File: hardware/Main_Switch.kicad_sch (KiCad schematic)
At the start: 6 parts

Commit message: Nightly update
Update Driver and Main_Switch.
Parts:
- added R? (x10): (no value), symbol Basic_passive_components:Resistor
- L?: value Power_Inductor -> (none)
- Q? (x4): value NTMFS5C670NL -> (none); footprint POWER_TRANSISTOR_SMD:SON-8_5x6_M -> (none)
- R?: value Resistor -> (none)
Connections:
- net BG1: now also R?.1; no longer Q?.G (Gate)
- net BG2: now also R?.2; no longer Q?.G (Gate)
- net GND: now also Q?.S (Source), Q?.S (Source), R?.1, R?.1
- net TG1: now also R?.1; no longer Q?.G (Gate)
- net TG2: now also R?.2; no longer Q?.G (Gate)
- net VBUS: now also Q?.D (Drain)
- net VDC: now also Q?.D (Drain)
- net SW2: now reaches Q?.D (Drain), Q?.S (Source), R?.2
- net SW2: now also R?.1, R?.2
- net SW1: now reaches L?.1, Q?.D (Drain), Q?.S (Source)
- net SW1: now also R?.1
- net at L?.2, R?.1: now also R?.2
- new net: Q?.G (Gate), R?.1, R?.2 (x2)
- new net: Q?.G (Gate), R?.2, R?.2 (x2)
- new net CS_N: R?.1
- new net CS_P: R?.1
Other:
- moved on the sheet: Q?

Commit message: Nightly update
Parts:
- L?: value (none) -> 4.7uH; footprint (none) -> POWER_INDUCTOR_SMD:MC-1770
- Q? (x4): value (none) -> NTMFS5C670NL; footprint (none) -> POWER_TRANSISTOR_SMD:SON-8_5x6_M
- R? (x4): value (none) -> 10kR; footprint (none) -> GENERAL_RCL_SMD:R0603(1608M)
- R? (x2): value (none) -> 0R; footprint (none) -> GENERAL_RCL_SMD:R0402(1005M)
- R? (x4): value (none) -> 5.1R; footprint (none) -> GENERAL_RCL_SMD:R0603(1608M)
- R?: value (none) -> 10mR; footprint (none) -> GENERAL_RCL_SMD:R2512(6332M)
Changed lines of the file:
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@@
       (effects (font (size 1.27 1.27)) (justify left))
     )
-    (property "Value" "" (id 1) (at 175.26 102.8699 0)
-      (effects (font (size 1.27 1.27)) (justify left))
-    )
-    (property "Footprint" "" (id 2) (at 156.21 97.79 0)
+    (property "Value" "NTMFS5C670NL" (id 1) (at 175.26 102.8699 0)
+      (effects (font (size 1.27 1.27)) (justify left))
+    )
+    (property "Footprint" "POWER_TRANSISTOR_SMD:SON-8_5x6_M" (id 2) (at 156.21 97.79 0)
       (effects (font (size 1.27 1.27)) hide)
     )
@@
       (effects (font (size 1.27 1.27)) (justify right))
     )
-    (property "Value" "" (id 1) (at 96.52 110.4899 90)
-      (effects (font (size 1.27 1.27)) (justify right))
-    )
-    (property "Footprint" "" (id 2) (at 90.17 113.03 0)
+    (property "Value" "10kR" (id 1) (at 96.52 110.4899 90)
+      (effects (font (size 1.27 1.27)) (justify right))
+    )
+    (property "Footprint" "GENERAL_RCL_SMD:R0603(1608M)" (id 2) (at 90.17 113.03 0)
       (effects (font (size 1.27 1.27)) hide)
     )
@@
     (in_bom yes) (on_board yes) (fields_autoplaced)
     (property "Reference" "R?" (id 0) (at 137.16 105.41 0))
-    (property "Value" "" (id 1) (at 137.16 107.95 0))
-    (property "Footprint" "" (id 2) (at 133.35 107.95 0)
+    (property "Value" "0R" (id 1) (at 137.16 107.95 0))
+    (property "Footprint" "GENERAL_RCL_SMD:R0402(1005M)" (id 2) (at 133.35 107.95 0)
       (effects (font (size 1.27 1.27)) hide)
     )
@@
       (effects (font (size 1.27 1.27)) (justify right))
     )
-    (property "Value" "" (id 1) (at 96.52 72.3899 90)
-      (effects (font (size 1.27 1.27)) (justify right))
-    )
-    (property "Footprint" "" (id 2) (at 90.17 74.93 0)
+    (property "Value" "10kR" (id 1) (at 96.52 72.3899 90)
+      (effects (font (size 1.27 1.27)) (justify right))
+    )
+    (property "Footprint" "GENERAL_RCL_SMD:R0603(1608M)" (id 2) (at 90.17 74.93 0)
       (effects (font (size 1.27 1.27)) hide)
     )
@@
       (effects (font (size 1.27 1.27)) (justify left))
     )
-    (property "Value" "" (id 1) (at 104.14 64.7699 0)
-      (effects (font (size 1.27 1.27)) (justify left))
-    )
-    (property "Footprint" "" (id 2) (at 123.19 59.69 0)
+    (property "Value" "NTMFS5C670NL" (id 1) (at 104.14 64.7699 0)
+      (effects (font (size 1.27 1.27)) (justify left))
+    )
+    (property "Footprint" "POWER_TRANSISTOR_SMD:SON-8_5x6_M" (id 2) (at 123.19 59.69 0)
       (effects (font (size 1.27 1.27)) hide)
     )
@@
       (effects (font (size 1.27 1.27)) (justify left))
     )
-    (property "Value" "" (id 1) (at 175.26 64.7699 0)
-      (effects (font (size 1.27 1.27)) (justify left))
-    )
-    (property "Footprint" "" (id 2) (at 156.21 59.69 0)
+    (property "Value" "NTMFS5C670NL" (id 1) (at 175.26 64.7699 0)
+      (effects (font (size 1.27 1.27)) (justify left))
+    )
+    (property "Footprint" "POWER_TRANSISTOR_SMD:SON-8_5x6_M" (id 2) (at 156.21 59.69 0)
       (effects (font (size 1.27 1.27)) hide)
     )
@@
     (in_bom yes) (on_board yes) (fields_autoplaced)
     (property "Reference" "R?" (id 0) (at 195.58 95.25 0))
-    (property "Value" "" (id 1) (at 195.58 97.79 0))
-    (property "Footprint" "" (id 2) (at 191.77 97.79 0)
+    (property "Value" "5.1R" (id 1) (at 195.58 97.79 0))
+    (property "Footprint" "GENERAL_RCL_SMD:R0603(1608M)" (id 2) (at 191.77 97.79 0)
       (effects (font (size 1.27 1.27)) hide)
     )
@@
       (effects (font (size 1.27 1.27)) (justify left))
     )
-    (property "Value" "" (id 1) (at 104.14 102.8699 0)
-      (effects (font (size 1.27 1.27)) (justify left))
-    )
-    (property "Footprint" "" (id 2) (at 123.19 97.79 0)
+    (property "Value" "NTMFS5C670NL" (id 1) (at 104.14 102.8699 0)
+      (effects (font (size 1.27 1.27)) (justify left))
+    )
+    (property "Footprint" "POWER_TRANSISTOR_SMD:SON-8_5x6_M" (id 2) (at 123.19 97.79 0)
       (effects (font (size 1.27 1.27)) hide)
     )
@@
       (effects (font (size 1.27 1.27)) (justify right))
     )
-    (property "Value" "" (id 1) (at 190.5 110.4899 90)
-      (effects (font (size 1.27 1.27)) (justify right))
-    )
-    (property "Footprint" "" (id 2) (at 184.15 113.03 0)
+    (property "Value" "10kR" (id 1) (at 190.5 110.4899 90)
+      (effects (font (size 1.27 1.27)) (justify right))
+    )
+    (property "Footprint" "GENERAL_RCL_SMD:R0603(1608M)" (id 2) (at 184.15 113.03 0)
       (effects (font (size 1.27 1.27)) hide)
     )
@@
     (in_bom yes) (on_board yes) (fields_autoplaced)
     (property "Reference" "L?" (id 0) (at 127 82.55 0))
-    (property "Value" "" (id 1) (at 127 85.09 0))
-    (property "Footprint" "" (id 2) (at 127 88.9 0)
+    (property "Value" "4.7uH" (id 1) (at 127 85.09 0))
+    (property "Footprint" "POWER_INDUCTOR_SMD:MC-1770" (id 2) (at 127 88.9 0)
       (effects (font (size 1.27 1.27)) hide)
     )
@@
       (effects (font (size 1.27 1.27)) hide)
     )
-    (property "Value" "" (id 1) (at 177.8 132.08 0))
+    (property "Value" "GND" (id 1) (at 177.8 132.08 0))
     (property "Footprint" "" (id 2) (at 177.8 127 0)
       (effects (font (size 1.27 1.27)) hide)
@@
     (in_bom yes) (on_board yes) (fields_autoplaced)
     (property "Reference" "R?" (id 0) (at 83.82 57.15 0))
-    (property "Value" "" (id 1) (at 83.82 59.69 0))
-    (property "Footprint" "" (id 2) (at 80.01 59.69 0)
+    (property "Value" "5.1R" (id 1) (at 83.82 59.69 0))
+    (property "Footprint" "GENERAL_RCL_SMD:R0603(1608M)" (id 2) (at 80.01 59.69 0)
       (effects (font (size 1.27 1.27)) hide)
     )
@@
     (in_bom yes) (on_board yes) (fields_autoplaced)
     (property "Reference" "R?" (id 0) (at 137.16 95.25 0))
-    (property "Value" "" (id 1) (at 137.16 97.79 0))
-    (property "Footprint" "" (id 2) (at 133.35 97.79 0)
+    (property "Value" "0R" (id 1) (at 137.16 97.79 0))
+    (property "Footprint" "GENERAL_RCL_SMD:R0402(1005M)" (id 2) (at 133.35 97.79 0)
       (effects (font (size 1.27 1.27)) hide)
     )
@@
       (effects (font (size 1.27 1.27)) hide)
     )
-    (property "Value" "" (id 1) (at 101.6 45.72 0))
+    (property "Value" "VDC" (id 1) (at 101.6 45.72 0))
     (property "Footprint" "" (id 2) (at 101.6 50.8 0)
       (effects (font (size 1.27 1.27)) hide)
@@
     (in_bom yes) (on_board yes) (fields_autoplaced)
     (property "Reference" "R?" (id 0) (at 152.4 82.55 0))
-    (property "Value" "" (id 1) (at 152.4 85.09 0))
-    (property "Footprint" "" (id 2) (at 148.59 85.09 0)
+    (property "Value" "10mR" (id 1) (at 152.4 85.09 0))
+    (property "Footprint" "GENERAL_RCL_SMD:R2512(6332M)" (id 2) (at 148.59 85.09 0)
       (effects (font (size 1.27 1.27)) hide)
     )
@@
       (effects (font (size 1.27 1.27)) hide)
     )
-    (property "Value" "" (id 1) (at 177.8 45.72 0))
+    (property "Value" "VBUS" (id 1) (at 177.8 45.72 0))
     (property "Footprint" "" (id 2) (at 177.8 50.8 0)
       (effects (font (size 1.27 1.27)) hide)
@@
     (in_bom yes) (on_board yes) (fields_autoplaced)
     (property "Reference" "R?" (id 0) (at 195.58 57.15 0))
-    (property "Value" "" (id 1) (at 195.58 59.69 0))
-    (property "Footprint" "" (id 2) (at 191.77 59.69 0)
+    (property "Value" "5.1R" (id 1) (at 195.58 59.69 0))
+    (property "Footprint" "GENERAL_RCL_SMD:R0603(1608M)" (id 2) (at 191.77 59.69 0)
       (effects (font (size 1.27 1.27)) hide)
     )
@@
       (effects (font (size 1.27 1.27)) (justify right))
     )
-    (property "Value" "" (id 1) (at 190.5 72.3899 90)
-      (effects (font (size 1.27 1.27)) (justify right))
-    )
-    (property "Footprint" "" (id 2) (at 184.15 74.93 0)
+    (property "Value" "10kR" (id 1) (at 190.5 72.3899 90)
+      (effects (font (size 1.27 1.27)) (justify right))
+    )
+    (property "Footprint" "GENERAL_RCL_SMD:R0603(1608M)" (id 2) (at 184.15 74.93 0)
       (effects (font (size 1.27 1.27)) hide)
     )
@@
     (in_bom yes) (on_board yes) (fields_autoplaced)
     (property "Reference" "R?" (id 0) (at 83.82 95.25 0))
-    (property "Value" "" (id 1) (at 83.82 97.79 0))
-    (property "Footprint" "" (id 2) (at 80.01 97.79 0)
+    (property "Value" "5.1R" (id 1) (at 83.82 97.79 0))
+    (property "Footprint" "GENERAL_RCL_SMD:R0603(1608M)" (id 2) (at 80.01 97.79 0)
       (effects (font (size 1.27 1.27)) hide)
     )
@@
       (effects (font (size 1.27 1.27)) hide)
     )
-    (property "Value" "" (id 1) (at 101.6 132.08 0))
+    (property "Value" "GND" (id 1) (at 101.6 132.08 0))
     (property "Footprint" "" (id 2) (at 101.6 127 0)
       (effects (font (size 1.27 1.27)) hide)

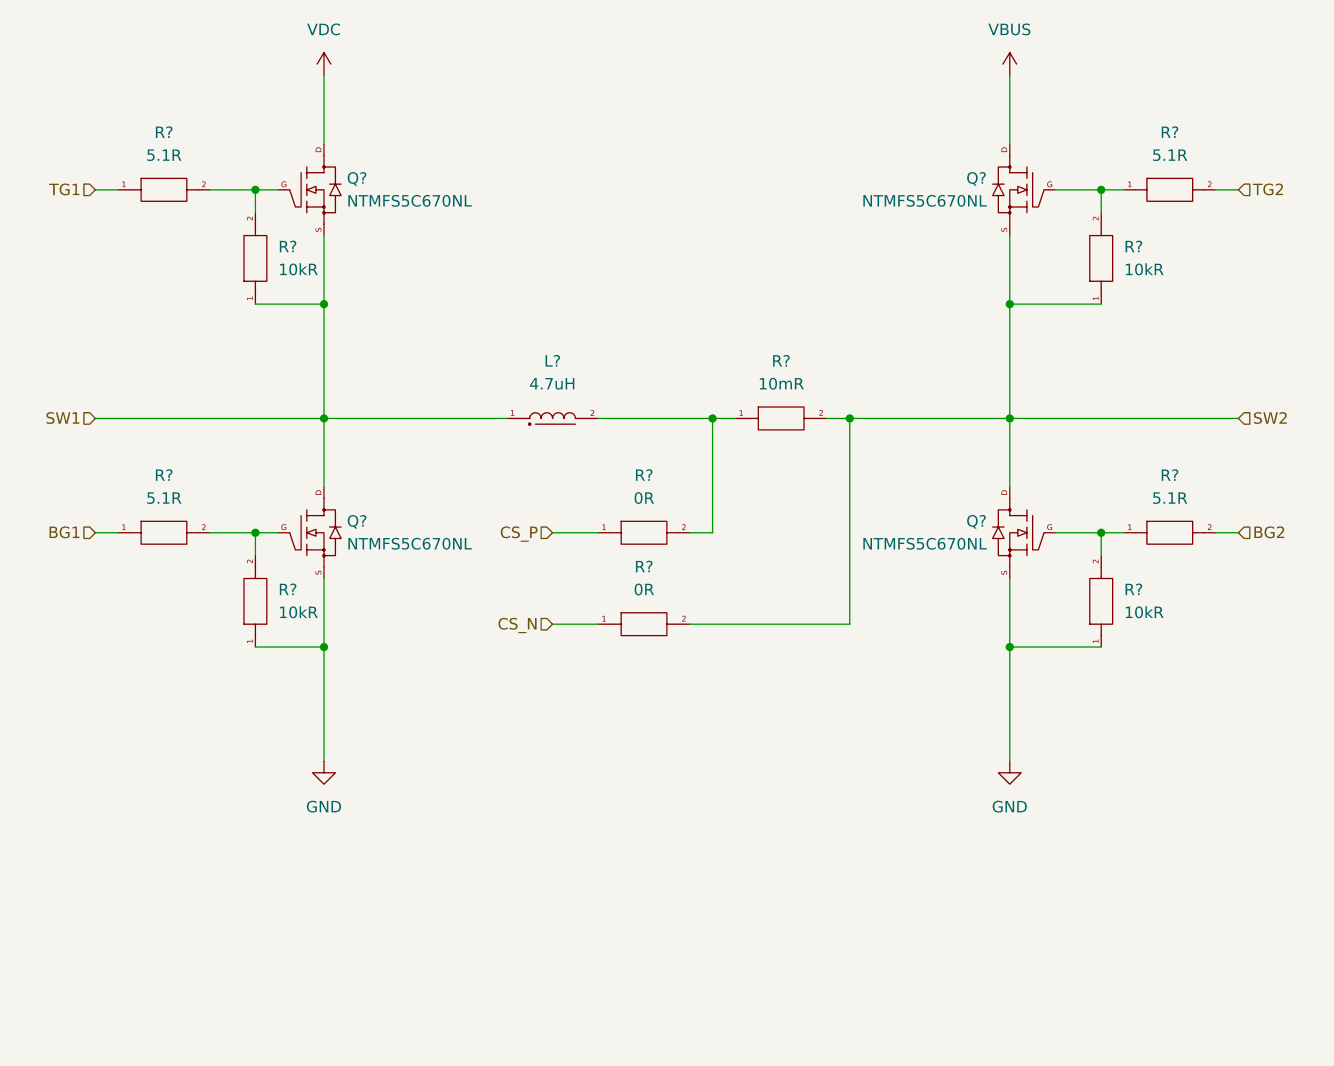
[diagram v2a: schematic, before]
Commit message: Update symbols
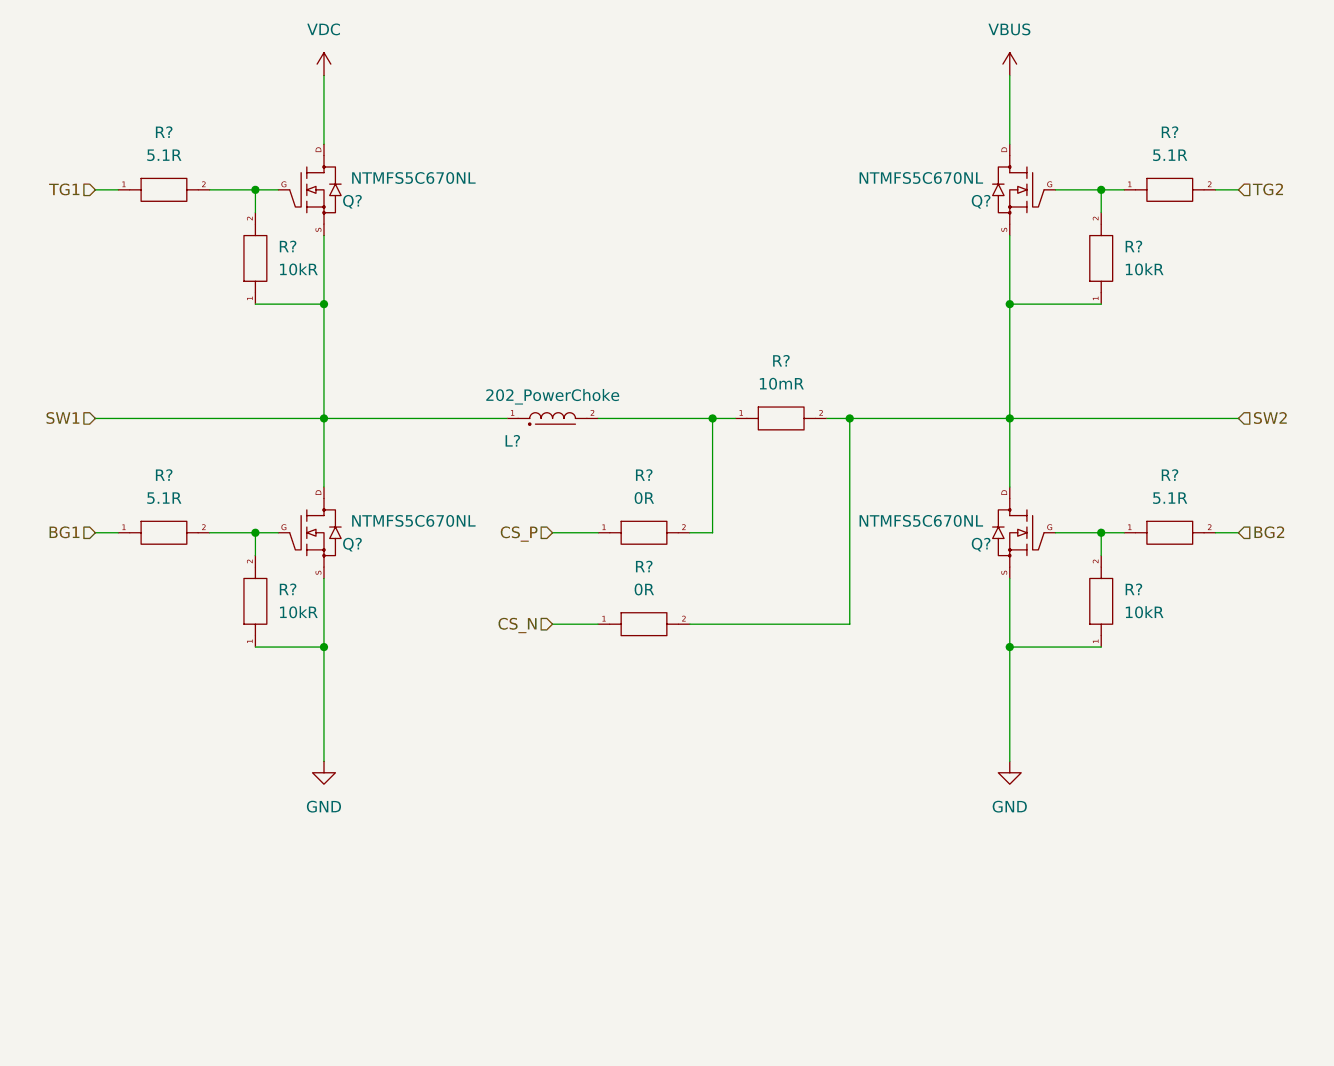
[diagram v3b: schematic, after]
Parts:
- L?: value 4.7uH -> 202_PowerChoke; symbol Basic_passive_components:Power_Inductor -> 001_Basic_PassiveComponents:202_PowerChoke; Symbol type (none) -> Alternate Source
- Q? (x4): footprint POWER_TRANSISTOR_SMD:SON-8_5x6_M -> 103_SP_POWER_TRANSISTOR_SMD:SON-6050-FET; symbol Power_transistor:NTMFS5C670NL -> 202_Power_Transistor:NTMFS5C670NL; Symbol type (none) -> Specified Device
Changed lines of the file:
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@@
     (effects (font (size 1.27 1.27)) (justify left))
   )
-  (symbol (lib_id "Power_transistor:NTMFS5C670NL") (at 177.8 101.6 0) (mirror y) (unit 1)
+  (symbol (lib_id "202_Power_Transistor:NTMFS5C670NL") (at 177.8 101.6 0) (mirror y) (unit 1)
     (in_bom yes) (on_board yes) (fields_autoplaced)
-    (property "Reference" "Q?" (id 0) (at 175.26 100.3299 0)
-      (effects (font (size 1.27 1.27)) (justify left))
-    )
-    (property "Value" "NTMFS5C670NL" (id 1) (at 175.26 102.8699 0)
-      (effects (font (size 1.27 1.27)) (justify left))
-    )
-    (property "Footprint" "POWER_TRANSISTOR_SMD:SON-8_5x6_M" (id 2) (at 156.21 97.79 0)
+    (property "Reference" "Q?" (id 0) (at 174.625 102.87 0))
+    (property "Value" "NTMFS5C670NL" (id 1) (at 167.894 100.33 0))
+    (property "Footprint" "103_SP_POWER_TRANSISTOR_SMD:SON-6050-FET" (id 2) (at 151.13 97.79 0)
       (effects (font (size 1.27 1.27)) hide)
     )
     (property "Datasheet" "" (id 3) (at 177.165 101.6 0)
+      (effects (font (size 1.27 1.27)) hide)
+    )
+    (property "Symbol type" "Specified Device" (id 4) (at 167.64 95.25 0)
       (effects (font (size 1.27 1.27)) hide)
     )
@@
     (pin "2")
   )
-  (symbol (lib_id "Power_transistor:NTMFS5C670NL") (at 101.6 63.5 0) (unit 1)
+  (symbol (lib_id "202_Power_Transistor:NTMFS5C670NL") (at 101.6 63.5 0) (unit 1)
     (in_bom yes) (on_board yes) (fields_autoplaced)
-    (property "Reference" "Q?" (id 0) (at 104.14 62.2299 0)
-      (effects (font (size 1.27 1.27)) (justify left))
-    )
-    (property "Value" "NTMFS5C670NL" (id 1) (at 104.14 64.7699 0)
-      (effects (font (size 1.27 1.27)) (justify left))
-    )
-    (property "Footprint" "POWER_TRANSISTOR_SMD:SON-8_5x6_M" (id 2) (at 123.19 59.69 0)
+    (property "Reference" "Q?" (id 0) (at 104.775 64.77 0))
+    (property "Value" "NTMFS5C670NL" (id 1) (at 111.506 62.23 0))
+    (property "Footprint" "103_SP_POWER_TRANSISTOR_SMD:SON-6050-FET" (id 2) (at 128.27 59.69 0)
       (effects (font (size 1.27 1.27)) hide)
     )
     (property "Datasheet" "" (id 3) (at 102.235 63.5 0)
+      (effects (font (size 1.27 1.27)) hide)
+    )
+    (property "Symbol type" "Specified Device" (id 4) (at 111.76 57.15 0)
       (effects (font (size 1.27 1.27)) hide)
     )
@@
     (pin "S")
   )
-  (symbol (lib_id "Power_transistor:NTMFS5C670NL") (at 177.8 63.5 0) (mirror y) (unit 1)
+  (symbol (lib_id "202_Power_Transistor:NTMFS5C670NL") (at 177.8 63.5 0) (mirror y) (unit 1)
     (in_bom yes) (on_board yes) (fields_autoplaced)
-    (property "Reference" "Q?" (id 0) (at 175.26 62.2299 0)
-      (effects (font (size 1.27 1.27)) (justify left))
-    )
-    (property "Value" "NTMFS5C670NL" (id 1) (at 175.26 64.7699 0)
-      (effects (font (size 1.27 1.27)) (justify left))
-    )
-    (property "Footprint" "POWER_TRANSISTOR_SMD:SON-8_5x6_M" (id 2) (at 156.21 59.69 0)
+    (property "Reference" "Q?" (id 0) (at 174.625 64.77 0))
+    (property "Value" "NTMFS5C670NL" (id 1) (at 167.894 62.23 0))
+    (property "Footprint" "103_SP_POWER_TRANSISTOR_SMD:SON-6050-FET" (id 2) (at 151.13 59.69 0)
       (effects (font (size 1.27 1.27)) hide)
     )
     (property "Datasheet" "" (id 3) (at 177.165 63.5 0)
+      (effects (font (size 1.27 1.27)) hide)
+    )
+    (property "Symbol type" "Specified Device" (id 4) (at 167.64 57.15 0)
       (effects (font (size 1.27 1.27)) hide)
     )
@@
     (pin "2")
   )
-  (symbol (lib_id "Power_transistor:NTMFS5C670NL") (at 101.6 101.6 0) (unit 1)
+  (symbol (lib_id "202_Power_Transistor:NTMFS5C670NL") (at 101.6 101.6 0) (unit 1)
     (in_bom yes) (on_board yes) (fields_autoplaced)
-    (property "Reference" "Q?" (id 0) (at 104.14 100.3299 0)
-      (effects (font (size 1.27 1.27)) (justify left))
-    )
-    (property "Value" "NTMFS5C670NL" (id 1) (at 104.14 102.8699 0)
-      (effects (font (size 1.27 1.27)) (justify left))
-    )
-    (property "Footprint" "POWER_TRANSISTOR_SMD:SON-8_5x6_M" (id 2) (at 123.19 97.79 0)
+    (property "Reference" "Q?" (id 0) (at 104.775 102.87 0))
+    (property "Value" "NTMFS5C670NL" (id 1) (at 111.506 100.33 0))
+    (property "Footprint" "103_SP_POWER_TRANSISTOR_SMD:SON-6050-FET" (id 2) (at 128.27 97.79 0)
       (effects (font (size 1.27 1.27)) hide)
     )
     (property "Datasheet" "" (id 3) (at 102.235 101.6 0)
+      (effects (font (size 1.27 1.27)) hide)
+    )
+    (property "Symbol type" "Specified Device" (id 4) (at 111.76 95.25 0)
       (effects (font (size 1.27 1.27)) hide)
     )
@@
     (pin "2")
   )
-  (symbol (lib_id "Basic_passive_components:Power_Inductor") (at 127 88.9 0) (unit 1)
+  (symbol (lib_id "001_Basic_PassiveComponents:202_PowerChoke") (at 127 88.9 0) (unit 1)
     (in_bom yes) (on_board yes) (fields_autoplaced)
-    (property "Reference" "L?" (id 0) (at 127 82.55 0))
-    (property "Value" "4.7uH" (id 1) (at 127 85.09 0))
+    (property "Reference" "L?" (id 0) (at 122.555 91.44 0))
+    (property "Value" "202_PowerChoke" (id 1) (at 127 86.36 0))
     (property "Footprint" "POWER_INDUCTOR_SMD:MC-1770" (id 2) (at 127 88.9 0)
       (effects (font (size 1.27 1.27)) hide)
@@
       (effects (font (size 1.27 1.27)) hide)
     )
+    (property "Symbol type" "Alternate Source" (id 4) (at 127 83.82 0)
+      (effects (font (size 1.27 1.27)) hide)
+    )
